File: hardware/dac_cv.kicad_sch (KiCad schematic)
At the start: 16 parts, among them J6 CV_OUT_T1, J7 CV_OUT_T3, J8 CV_OUT_T2, U5 Opamp_Quad

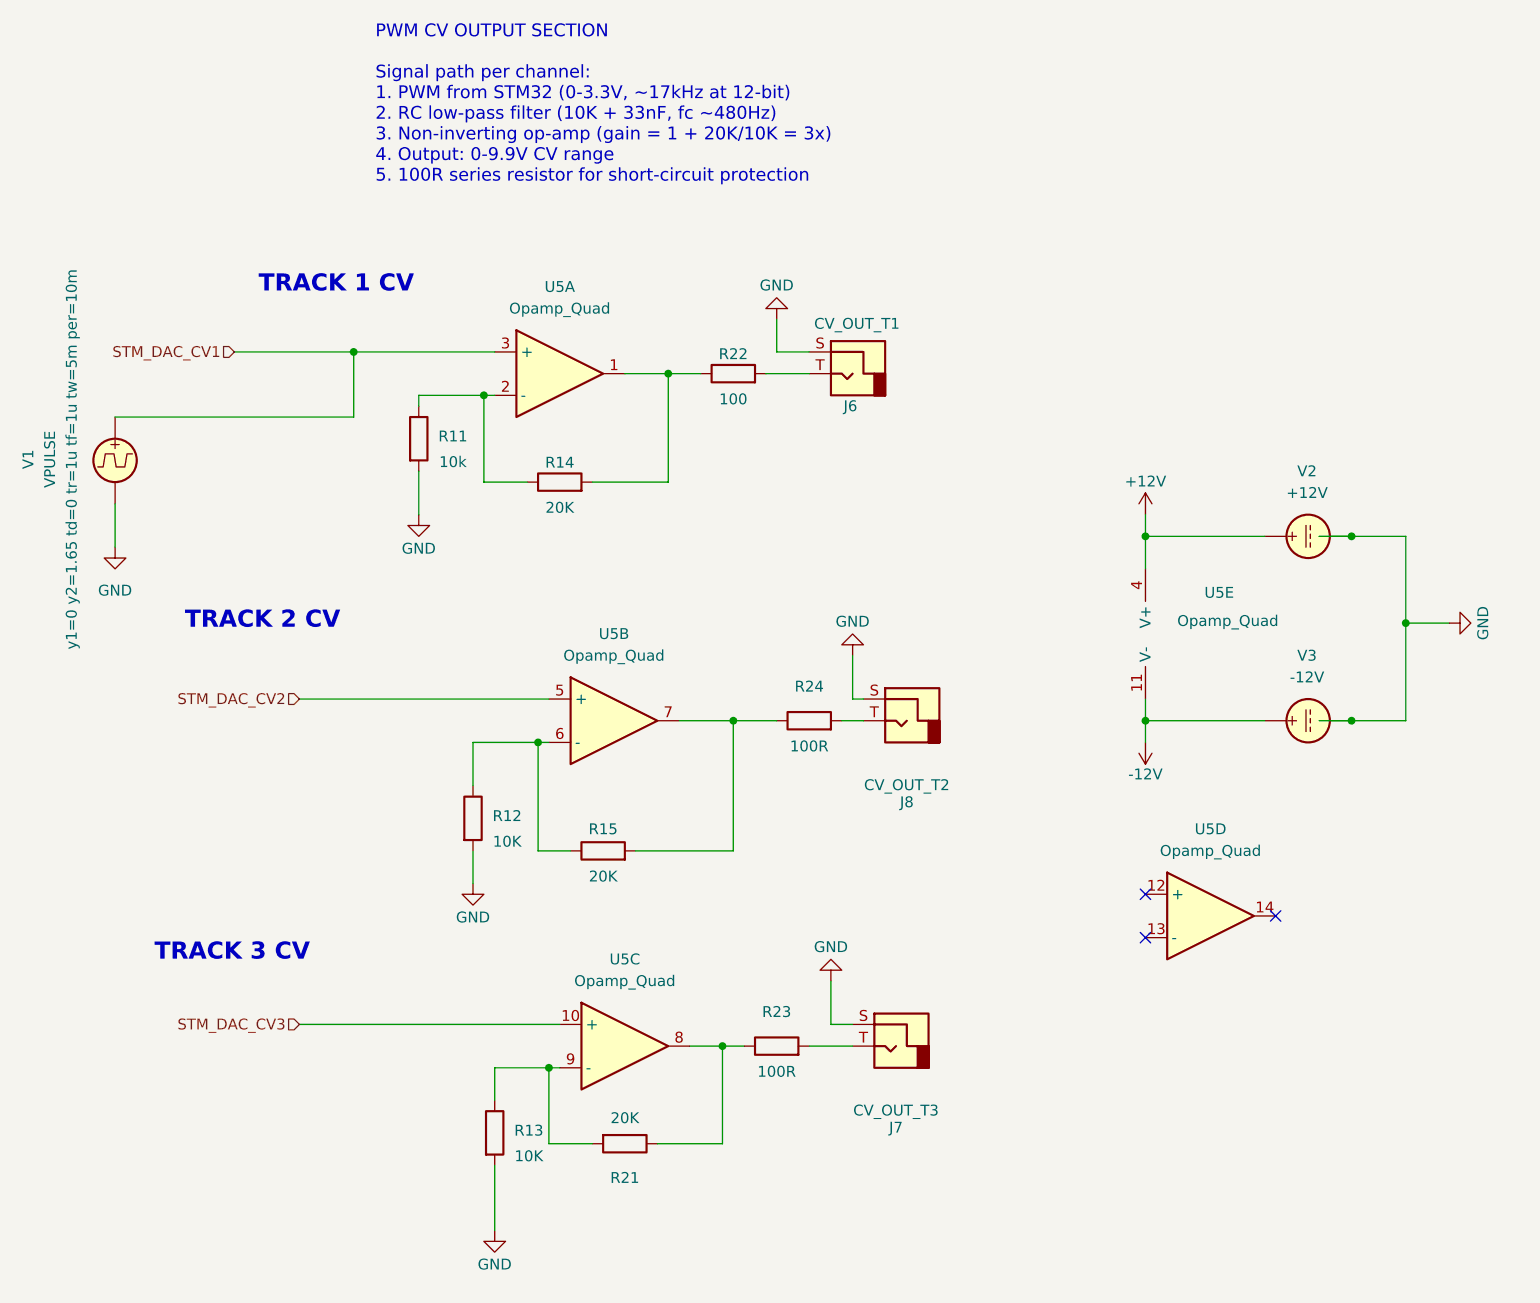
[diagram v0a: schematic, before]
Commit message: Complete hierarchical schematic sheets and fix wiring
- Complete encoder_leds sheet with MAX7219 + 64 LEDs
- Complete ui_leds sheet with MAX7219 + 45 LEDs
- Complete buttons sheet with MCP23017 + 40 buttons
- Complete display sheet with OLED I2C connector
- Complete pots sheet with 3 potentiometers
- Complete encoders sheet with 8 rotary encoders on MCP23017
- Fix inputs sheet hierarchical labels (CLK_IN, RST_IN, SCENE_CV_IN)
- Update MCU sheet with ADC hierarchical labels
- Update root sheet with hierarchical pin connections
- Various ERC fixes and wiring corrections

Co-Authored-By: Claude Opus 4.5 <noreply@anthropic.com>
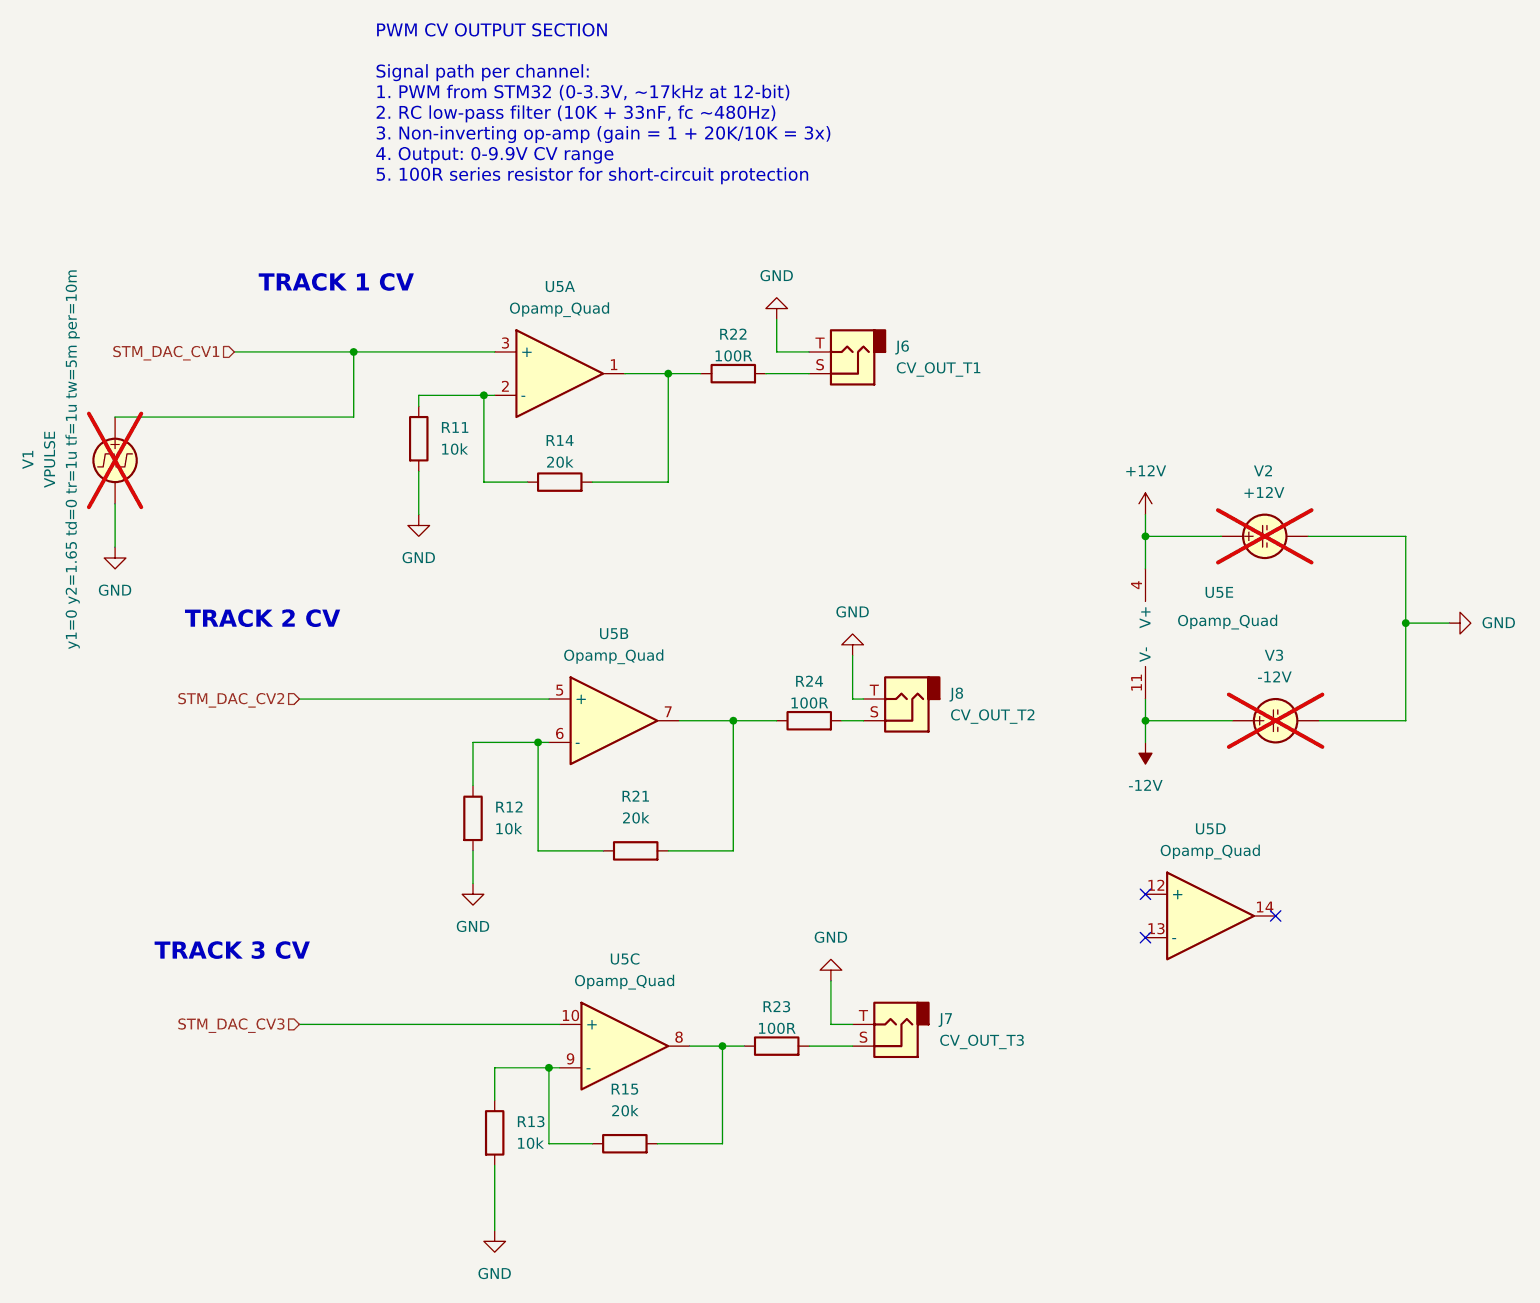
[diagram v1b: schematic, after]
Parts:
- removed J6: CV_OUT_T1, Connector_Audio:Jack_3.5mm_QingPu_WQP-PJ398SM_Vertical_CircularHoles, symbol Connector:AudioJack2
- removed J7: CV_OUT_T3, Connector_Audio:Jack_3.5mm_QingPu_WQP-PJ398SM_Vertical_CircularHoles, symbol Connector:AudioJack2
- removed J8: CV_OUT_T2, Connector_Audio:Jack_3.5mm_QingPu_WQP-PJ398SM_Vertical_CircularHoles, symbol Connector:AudioJack2
- added J6: CV_OUT_T1, symbol Connector_Audio:AudioJack2
- added J7: CV_OUT_T3, symbol Connector_Audio:AudioJack2
- added J8: CV_OUT_T2, symbol Connector_Audio:AudioJack2
- R11, R23, R24: footprint Resistor_SMD:R_0805_2012Metric -> (none)
- R12, R13: value 10K -> 10k; footprint Resistor_SMD:R_0805_2012Metric -> (none)
- R14, R15, R21: value 20K -> 20k; footprint Resistor_SMD:R_0805_2012Metric -> (none)
- R22: value 100 -> 100R; footprint Resistor_SMD:R_0805_2012Metric -> (none)
- V1, V2, V3: now not fitted; now left out of the parts list
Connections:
- net GND: now also J6.T, J7.T, J8.T
- net at R12.1, U5.6 (-): now also R21.1; no longer R15.1
- net at R24.1, U5.7: now also R21.2; no longer R15.2
- net at R24.2: now also J8.S
- net at R22.2: now also J6.S
- net at R23.1, U5.8: now also R15.2; no longer R21.1
- net at R23.2: now also J7.S
- net at R13.1, U5.9 (-): now also R15.1; no longer R21.2

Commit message: Assign footprints to all schematic components
SMD footprints assigned:
- Capacitors: 0402 (20pF), 0603 (100nF), 0805 (10uF), 1206 (47uF, 100uF)
- Resistors: 0603
- LEDs: 0201
- MAX7219: SOIC-24W
- ULN2003: SOIC-16
- Switches: TL3342 tactile
- Connectors: JST PH, pin headers

Also removes accidentally committed autosave files.

Co-Authored-By: Claude Opus 4.5 <noreply@anthropic.com>
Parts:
- J6, J7, J8: footprint (none) -> Connector_Audio:Jack_3.5mm_QingPu_WQP-PJ398SM_Vertical_CircularHoles
- R11, R12, R13, R14, R15, R21, R22, R23, R24: footprint (none) -> Resistor_SMD:R_0201_0603Metric_Pad0.64x0.40mm_HandSolder
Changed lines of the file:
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@@
 			)
 		)
-		(property "Footprint" ""
+		(property "Footprint" "Resistor_SMD:R_0201_0603Metric_Pad0.64x0.40mm_HandSolder"
 			(at 86.36 80.518 90)
 			(effects
@@
 			)
 		)
-		(property "Footprint" ""
+		(property "Footprint" "Resistor_SMD:R_0201_0603Metric_Pad0.64x0.40mm_HandSolder"
 			(at 74.422 118.11 90)
 			(effects
@@
 			)
 		)
-		(property "Footprint" ""
+		(property "Footprint" "Resistor_SMD:R_0201_0603Metric_Pad0.64x0.40mm_HandSolder"
 			(at 111.76 146.558 90)
 			(effects
@@
 			)
 		)
-		(property "Footprint" ""
+		(property "Footprint" "Resistor_SMD:R_0201_0603Metric_Pad0.64x0.40mm_HandSolder"
 			(at 115.57 108.458 90)
 			(effects
@@
 			)
 		)
-		(property "Footprint" ""
+		(property "Footprint" "Resistor_SMD:R_0201_0603Metric_Pad0.64x0.40mm_HandSolder"
 			(at 68.072 73.66 90)
 			(effects
@@
 			)
 		)
-		(property "Footprint" ""
+		(property "Footprint" "Resistor_SMD:R_0201_0603Metric_Pad0.64x0.40mm_HandSolder"
 			(at 106.68 67.818 90)
 			(effects
@@
 			)
 		)
-		(property "Footprint" ""
+		(property "Footprint" "Resistor_SMD:R_0201_0603Metric_Pad0.64x0.40mm_HandSolder"
 			(at 93.98 157.988 90)
 			(effects
@@
 			)
 		)
-		(property "Footprint" ""
+		(property "Footprint" "Resistor_SMD:R_0201_0603Metric_Pad0.64x0.40mm_HandSolder"
 			(at 76.962 154.94 90)
 			(effects
@@
 			)
 		)
-		(property "Footprint" ""
+		(property "Footprint" "Resistor_SMD:R_0201_0603Metric_Pad0.64x0.40mm_HandSolder"
 			(at 95.25 123.698 90)
 			(effects
@@
 			)
 		)
-		(property "Footprint" ""
+		(property "Footprint" "Connector_Audio:Jack_3.5mm_QingPu_WQP-PJ398SM_Vertical_CircularHoles"
 			(at 120.65 63.5 0)
 			(effects
@@
 			)
 		)
-		(property "Footprint" ""
+		(property "Footprint" "Connector_Audio:Jack_3.5mm_QingPu_WQP-PJ398SM_Vertical_CircularHoles"
 			(at 125.73 142.24 0)
 			(effects
@@
 			)
 		)
-		(property "Footprint" ""
+		(property "Footprint" "Connector_Audio:Jack_3.5mm_QingPu_WQP-PJ398SM_Vertical_CircularHoles"
 			(at 127 104.14 0)
 			(effects
